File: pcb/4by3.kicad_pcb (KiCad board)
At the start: 2 copper layers, 81 x 61.9 mm, 31 parts, among them K1 KEYSW, K10 KEYSW, K11 KEYSW, K12 KEYSW, K2 KEYSW, K3 KEYSW, K4 KEYSW, K5 KEYSW, K6 KEYSW, K7 KEYSW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

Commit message: Fixed pro micro pcb, created qmk firmware for the device
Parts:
- added ?: , Aesthetics:OSHW-LOGO-L, B.Cu at (160.7, 42.9)
- M1: footprint SparkFun-Boards:ARDUINO_PRO_MICRO -> Boards:SPARKFUN_PRO_MICRO
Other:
- board text added: "Rev 1"
- board text removed: "Rev 0"

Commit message: Changed text on pcb and wrote README.md
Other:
- board text added: "4by3"
- board text removed: "3by4"
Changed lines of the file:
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@@
     (effects (font (size 1.5 1.5) (thickness 0.3)) (justify mirror))
   )
-  (gr_text 3by4 (at 207.16875 40.48125) (layer B.SilkS)
+  (gr_text 4by3 (at 207.16875 40.48125) (layer B.SilkS)
     (effects (font (size 1.5 1.5) (thickness 0.3)) (justify mirror))
   )

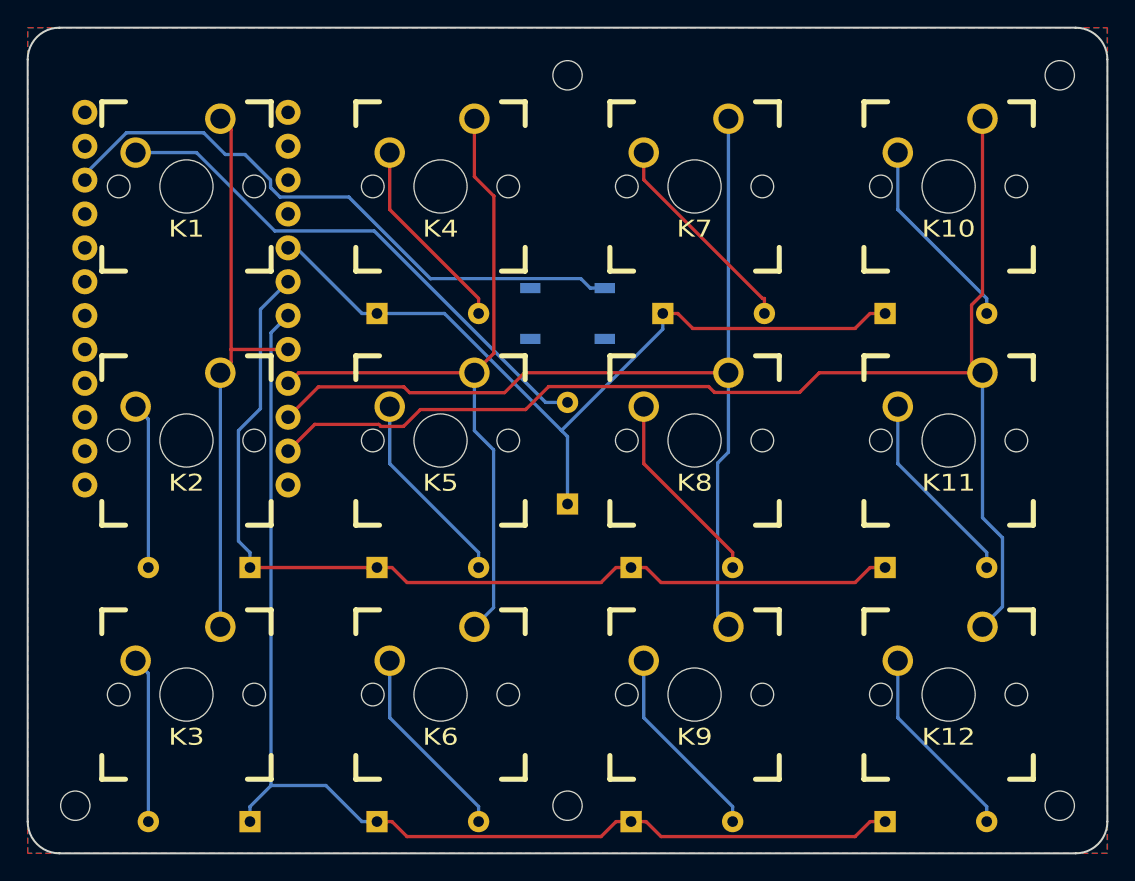
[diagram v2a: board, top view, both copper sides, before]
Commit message: Added images, created a pretty library
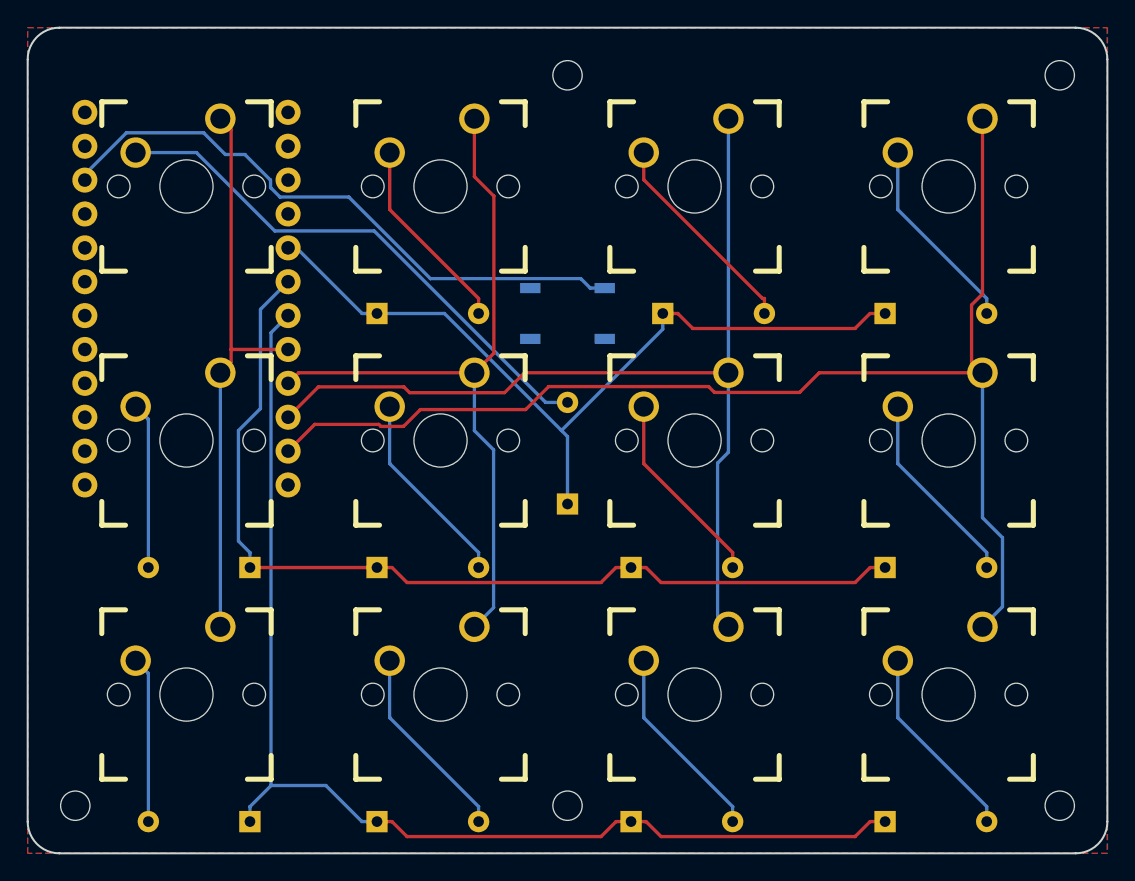
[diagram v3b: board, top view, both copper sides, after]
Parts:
- removed ?: , Aesthetics:OSHW-LOGO-L
- added >NAME: >VALUE, 4by3:OSHW_LOGO, B.Cu at (195.3, 44.1)
- added G: LOGO, 4by3:QMK_BADGE, B.Cu at (195.3, 54.8)
- added G***: LOGO, 4by3:4BY3_LOGO, B.Cu at (167.9, 85.7)
- D1, D10, D11, D12, D2, D3, D4, D5, D6, D7, D8, D9: footprint Diodes_THT:D_DO-35_SOD27_P7.62mm_Horizontal -> 4by3:DIODE
- H1, H2, H4, H5: value MountingHole_2.2mm_M2 -> (none); footprint Mounting_Holes:MountingHole_2.2mm_M2 -> 4by3:MOUNTING_HOLE
- H3: value MountingHole_2.2mm_M2 -> (none)
- K1, K10, K11, K12, K2, K3, K4, K5, K6, K7, K8, K9: footprint Keyboard:CHERRY_PCB_100H -> 4by3:CHERRY_MX_PCB
- M1: footprint Boards:SPARKFUN_PRO_MICRO -> 4by3:PRO_MICRO
- SW1: footprint Sparkfun_Switches:TACTILE_SWITCH_SMD_5.2MM -> 4by3:RESET_BUTTON
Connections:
- M1 pad 1: Net-(M1-Pad1) -> (no net)
- M1 pad 12: Net-(M1-Pad12) -> (no net)
- M1 pad 13: Net-(M1-Pad13) -> (no net)
- M1 pad 14: Net-(M1-Pad14) -> (no net)
- M1 pad 15: Net-(M1-Pad15) -> (no net)
- M1 pad 16: Net-(M1-Pad16) -> (no net)
- M1 pad 17: Net-(M1-Pad17) -> (no net)
- M1 pad 18: Net-(M1-Pad18) -> (no net)
- M1 pad 19: Net-(M1-Pad19) -> (no net)
- M1 pad 2: Net-(M1-Pad2) -> (no net)
- M1 pad 20: Net-(M1-Pad20) -> (no net)
- M1 pad 21: VCC -> (no net)
- M1 pad 24: Net-(M1-Pad24) -> (no net)
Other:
- board text added: "4by3 by Elias Sjögreen rev 1"
- board text removed: "4by3"
- board text removed: "Rev 1"
- board text removed: "by Elias Sjögreen"
